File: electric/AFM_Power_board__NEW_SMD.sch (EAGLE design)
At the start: 31 parts, among them IC2 7815DT, IC4 7805DT, J1 POWER_JACKPOWER_JACK_SLOT, U2 LTC3260EMSE#PBF

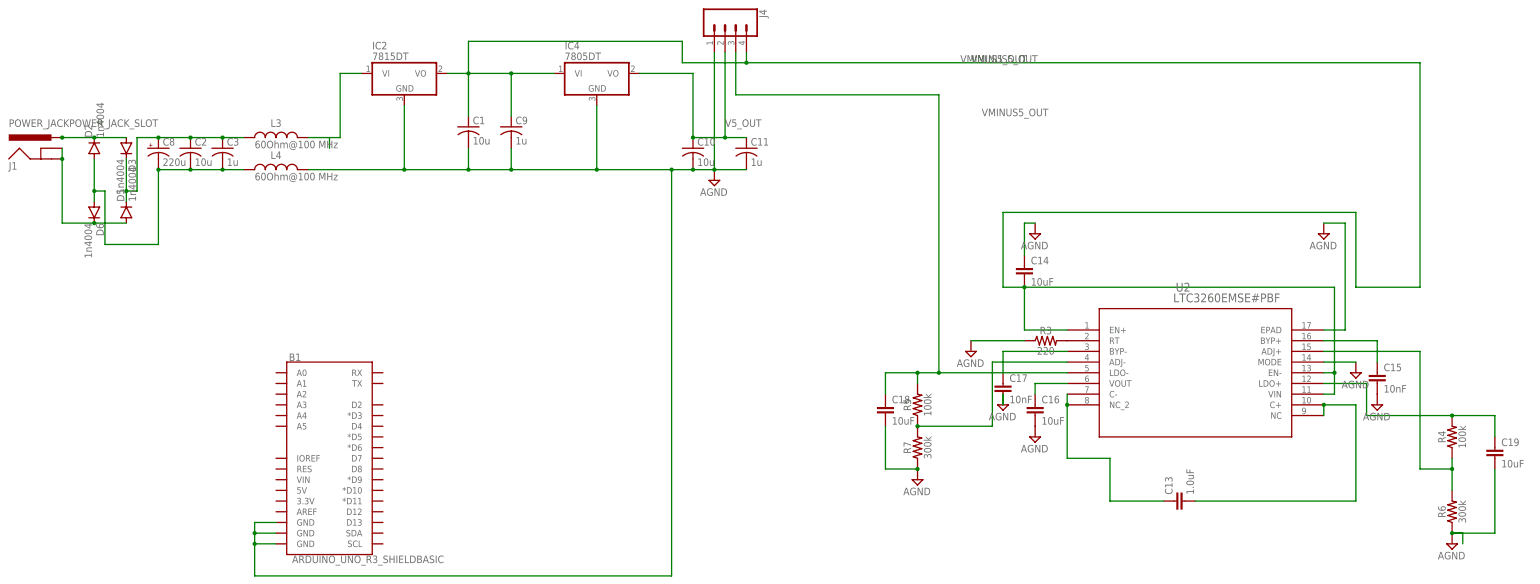
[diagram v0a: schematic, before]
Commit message: Updated to boards. Changes reflects fixes needed to PCBWay boards
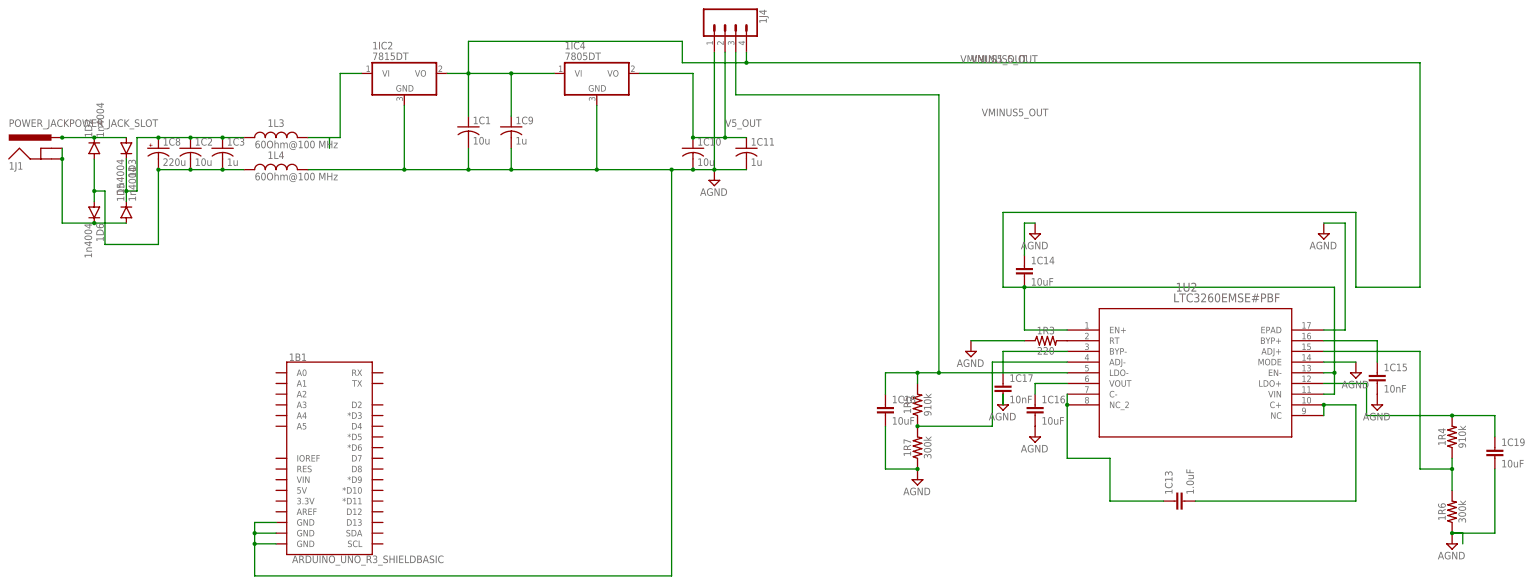
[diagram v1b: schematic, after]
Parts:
- 1R4, 1R5: value 100k -> 910k
- renumbered B1 to 1B1, C1 to 1C1, C10 to 1C10, C11 to 1C11, C13 to 1C13, C14 to 1C14, C15 to 1C15, C16 to 1C16, C17 to 1C17, C18 to 1C18, C19 to 1C19, C2 to 1C2, C3 to 1C3, C8 to 1C8, C9 to 1C9, D2 to 1D2, D3 to 1D3, D5 to 1D5, D6 to 1D6, IC2 to 1IC2, IC4 to 1IC4, J1 to 1J1, J4 to 1J4, L3 to 1L3, L4 to 1L4, R3 to 1R3, R4 to 1R4, R5 to 1R5, R6 to 1R6, R7 to 1R7, U2 to 1U2
